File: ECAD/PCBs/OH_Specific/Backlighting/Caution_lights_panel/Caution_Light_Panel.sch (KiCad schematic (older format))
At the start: 30 parts, among them J1 LedCathode, J2 LEDAnnode

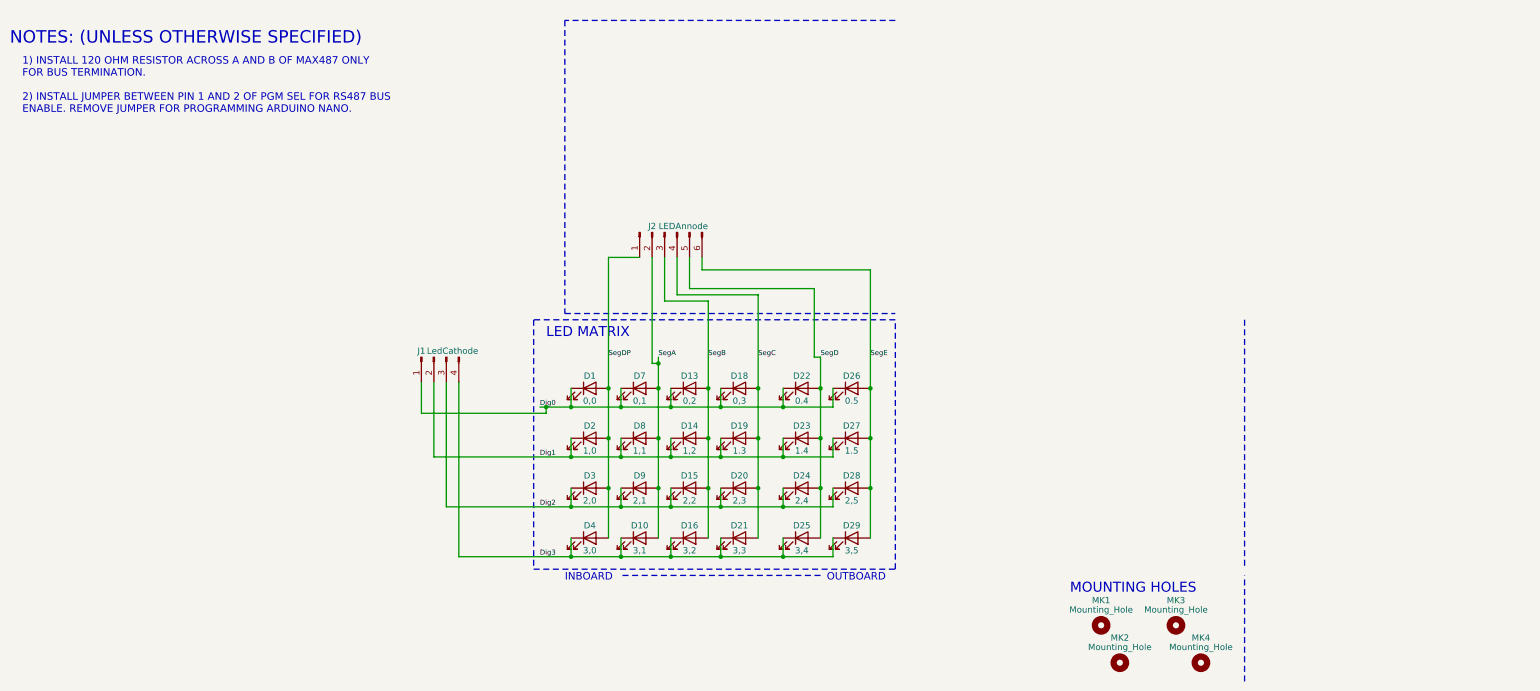
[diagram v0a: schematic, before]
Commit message: Defog Lever Backlighting
Added - Degfog Lever PCB ECAD Files
Added - Defog Lever PCB MCAD Model
Added - Holes in the backplate for the backlighting LEDs
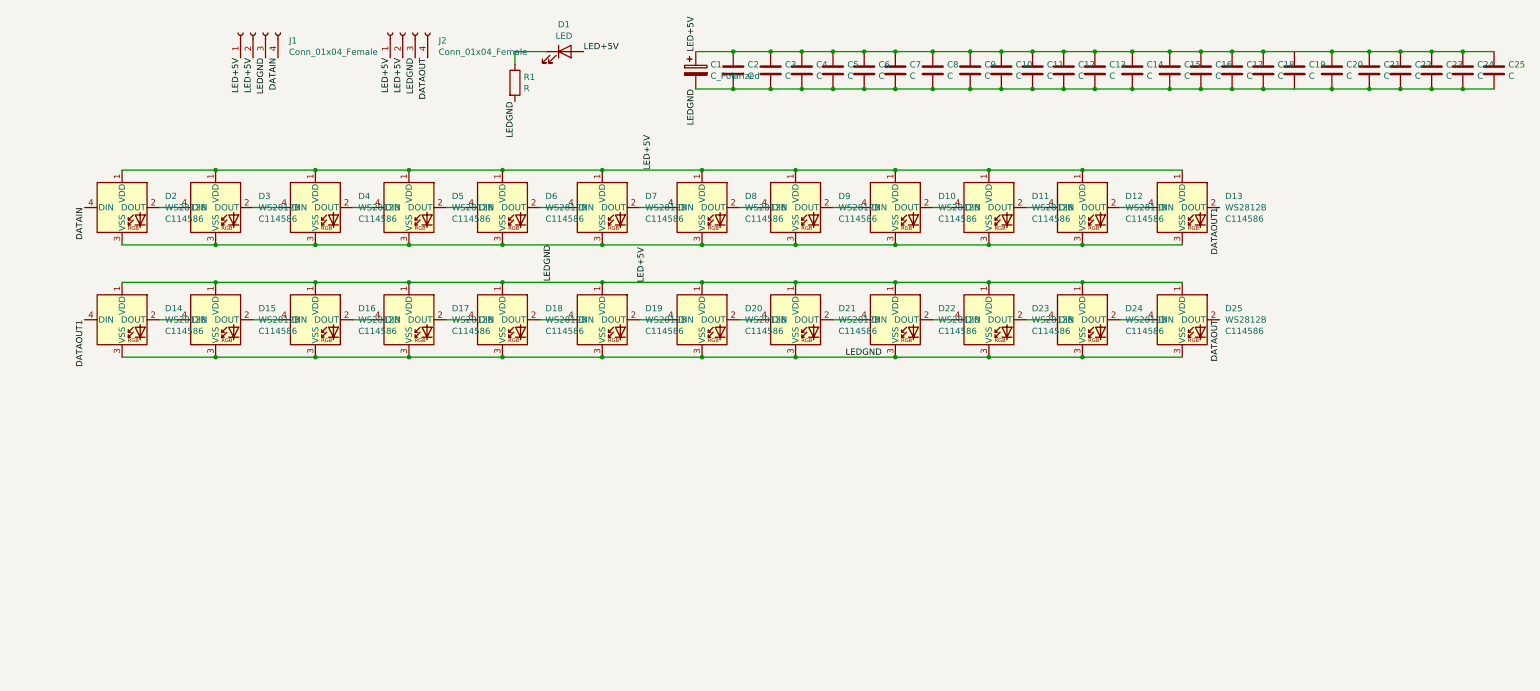
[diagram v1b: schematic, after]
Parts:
- removed D10: 3,1, LED_THT:LED_D3.0mm_FlatTop, symbol Device:LED
- removed D13: 0,2, LED_THT:LED_D3.0mm_FlatTop, symbol Device:LED
- removed D14: 1,2, LED_THT:LED_D3.0mm_FlatTop, symbol Device:LED
- removed D15: 2,2, LED_THT:LED_D3.0mm_FlatTop, symbol Device:LED
- removed D16: 3,2, LED_THT:LED_D3.0mm_FlatTop, symbol Device:LED
- removed D18: 0,3, LED_THT:LED_D3.0mm_FlatTop, symbol Device:LED
- removed D19: 1.3, LED_THT:LED_D3.0mm_FlatTop, symbol Device:LED
- removed D2: 1,0, LED_THT:LED_D3.0mm_FlatTop, symbol Device:LED
- removed D20: 2,3, LED_THT:LED_D3.0mm_FlatTop, symbol Device:LED
- removed D21: 3,3, LED_THT:LED_D3.0mm_FlatTop, symbol Device:LED
- removed D22: 0.4, LED_THT:LED_D3.0mm_FlatTop, symbol Device:LED
- removed D23: 1.4, LED_THT:LED_D3.0mm_FlatTop, symbol Device:LED
- removed D24: 2,4, LED_THT:LED_D3.0mm_FlatTop, symbol Device:LED
- removed D25: 3,4, LED_THT:LED_D3.0mm_FlatTop, symbol Device:LED
- removed D26: 0.5, LED_THT:LED_D3.0mm_FlatTop, symbol Device:LED
- removed D27: 1.5, LED_THT:LED_D3.0mm_FlatTop, symbol Device:LED
- removed D28: 2,5, LED_THT:LED_D3.0mm_FlatTop, symbol Device:LED
- removed D29: 3,5, LED_THT:LED_D3.0mm_FlatTop, symbol Device:LED
- removed D3: 2,0, LED_THT:LED_D3.0mm_FlatTop, symbol Device:LED
- removed D4: 3,0, LED_THT:LED_D3.0mm_FlatTop, symbol Device:LED
- removed D7: 0,1, LED_THT:LED_D3.0mm_FlatTop, symbol Device:LED
- removed D8: 1,1, LED_THT:LED_D3.0mm_FlatTop, symbol Device:LED
- removed D9: 2,1, LED_THT:LED_D3.0mm_FlatTop, symbol Device:LED
- removed J1: LedCathode, PT_Library_v001:Molex_1x04_P2.54mm_Vertical, symbol Connector:Conn_01x04_Male
- removed J2: LEDAnnode, PT_Library_v001:Molex_1x06_P2.54mm_Vertical, symbol Connector:Conn_01x06_Male
- removed MK1, MK2, MK3, MK4: Mounting_Hole, Mounting_Holes:MountingHole_2.5mm, symbol Mechanical:MountingHole
- added C1: C_Polarized, Capacitor_SMD:CP_Elec_8x10, symbol Device:C_Polarized
- added C10, C11, C12, C13, C14, C15, C16, C17, C18, C19, C2, C20, C21, C22, C23, C24, C25, C3, C4, C5, C6, C7, C8, C9: C, Capacitor_SMD:C_0603_1608Metric, symbol Device:C
- added D10, D11, D12, D13, D14, D15, D16, D17, D18, D19, D2, D20, D21, D22, D23, D24, D25, D3, D4, D5, D6, D7, D8, D9: WS2812B, LED_SMD:LED_WS2812B_PLCC4_5.0x5.0mm_P3.2mm, symbol LED:WS2812B
- added J1, J2: Conn_01x04_Female, Connector_Molex:Molex_Mini-Fit_Jr_5566-04A_2x02_P4.20mm_Vertical, symbol Connector:Conn_01x04_Female
- added R1: R, Resistor_SMD:R_0603_1608Metric, symbol Device:R
- D1: value 0,0 -> LED; footprint LED_THT:LED_D3.0mm_FlatTop -> LED_THT:LED_D3.0mm; PN IN-S63AT5UW -> (none)
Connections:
- net Dig0: no longer names the net of D1.1 (K)
- net Dig0: now also R1.1
- net SegDP renamed LED+5V
- net LED+5V: now also C1.1, C10.1, C11.1, C12.1, C13.1, C14.1, C15.1, C16.1, C17.1, C18.1, C19.1, C2.1, C20.1, C21.1, C22.1, C23.1, C24.1, C25.1, C3.1, C4.1, C5.1, C6.1, C7.1, C8.1, C9.1, D10.1 (VDD), D11.1 (VDD), D12.1 (VDD), D13.1 (VDD), D14.1 (VDD), D15.1 (VDD), D16.1 (VDD), D17.1 (VDD), D18.1 (VDD), D19.1 (VDD), D2.1 (VDD), D20.1 (VDD), D21.1 (VDD), D22.1 (VDD), D23.1 (VDD), D24.1 (VDD), D25.1 (VDD), D3.1 (VDD), D4.1 (VDD), D5.1 (VDD), D6.1 (VDD), D7.1 (VDD), D8.1 (VDD), D9.1 (VDD), J1.1 (Pin_1), J1.2 (Pin_2), J2.1 (Pin_1), J2.2 (Pin_2)
- new net: D2.2 (DOUT), D3.4 (DIN)
- new net: D3.2 (DOUT), D4.4 (DIN)
- new net: D4.2 (DOUT), D5.4 (DIN)
- new net: D5.2 (DOUT), D6.4 (DIN)
- new net: D6.2 (DOUT), D7.4 (DIN)
- new net: D7.2 (DOUT), D8.4 (DIN)
- new net: D8.2 (DOUT), D9.4 (DIN)
- new net: D10.4 (DIN), D9.2 (DOUT)
- new net: D10.2 (DOUT), D11.4 (DIN)
- new net: D11.2 (DOUT), D12.4 (DIN)
- new net: D12.2 (DOUT), D13.4 (DIN)
- new net: D14.2 (DOUT), D15.4 (DIN)
- new net: D15.2 (DOUT), D16.4 (DIN)
- new net: D16.2 (DOUT), D17.4 (DIN)
- new net: D17.2 (DOUT), D18.4 (DIN)
- new net: D18.2 (DOUT), D19.4 (DIN)
- new net: D19.2 (DOUT), D20.4 (DIN)
- new net: D20.2 (DOUT), D21.4 (DIN)
- new net: D21.2 (DOUT), D22.4 (DIN)
- new net: D22.2 (DOUT), D23.4 (DIN)
- new net: D23.2 (DOUT), D24.4 (DIN)
- new net: D24.2 (DOUT), D25.4 (DIN)
- new net DATAIN: D2.4 (DIN), J1.4 (Pin_4)
- new net DATAOUT: D25.2 (DOUT), J2.4 (Pin_4)
- new net DATAOUT1: D13.2 (DOUT), D14.4 (DIN)
- new net LEDGND: C1.2, C10.2, C11.2, C12.2, C13.2, C14.2, C15.2, C16.2, C17.2, C18.2, C19.2, C2.2, C20.2, C21.2, C22.2, C23.2, C24.2, C25.2, C3.2, C4.2, C5.2, C6.2, C7.2, C8.2, C9.2, D10.3 (VSS), D11.3 (VSS), D12.3 (VSS), D13.3 (VSS), D14.3 (VSS), D15.3 (VSS), D16.3 (VSS), D17.3 (VSS), D18.3 (VSS), D19.3 (VSS), D2.3 (VSS), D20.3 (VSS), D21.3 (VSS), D22.3 (VSS), D23.3 (VSS), D24.3 (VSS), D25.3 (VSS), D3.3 (VSS), D4.3 (VSS), D5.3 (VSS), D6.3 (VSS), D7.3 (VSS), D8.3 (VSS), D9.3 (VSS), J1.3 (Pin_3), J2.3 (Pin_3), R1.2
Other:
- note removed: "1) INSTALL 120 OHM RESISTOR ACROSS A AND B OF MAX487 ONLY \nFOR BUS TERMINATION.\n\n2) INSTALL JUMPER BETWEEN PIN 1 AND 2 OF PGM SEL FOR RS487 BUS \nENABLE. REMOVE JUMPER FOR PROGRAMMING ARDUINO NANO."
- note removed: "INBOARD"
- note removed: "LED MATRIX"
- note removed: "MOUNTING HOLES"
- note removed: "NOTES: (UNLESS OTHERWISE SPECIFIED)"
- note removed: "OUTBOARD"

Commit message: Latest backlighting changes
Update to multiple PCBs, mainly changing from micro-fit to mini-fit connectors.
Also changing from individual power rails to filled copper planes where possible.
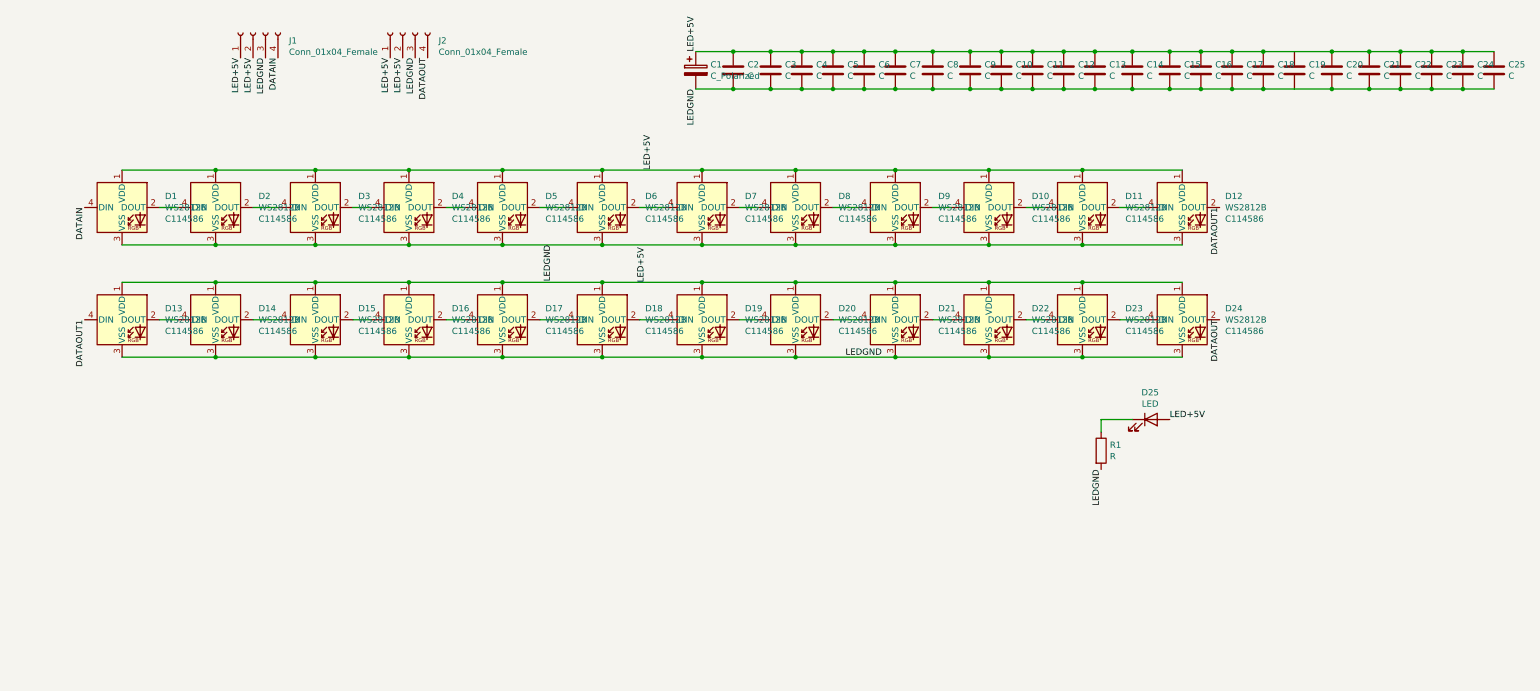
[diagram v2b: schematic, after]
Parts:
- renumbered D2 to D1, D11 to D10, D12 to D11, D13 to D12, D14 to D13, D15 to D14, D16 to D15, D17 to D16, D18 to D17, D19 to D18, D20 to D19, D3 to D2, D21 to D20, D22 to D21, D23 to D22, D24 to D23, D25 to D24, D1 to D25, D4 to D3, D5 to D4, D6 to D5, D7 to D6, D8 to D7, D9 to D8, D10 to D9
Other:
- moved on the sheet: D25, R1
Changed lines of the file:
@@
 L Device:R R1
 U 1 1 5FD9BD6D
-P 4650 1000
-F 0 "R1" H 4720 1046 50  0000 L CNN
-F 1 "R" H 4720 955 50  0000 L CNN
-F 2 "Resistor_SMD:R_0603_1608Metric" V 4580 1000 50  0001 C CNN
-F 3 "~" H 4650 1000 50  0001 C CNN
-	1    4650 1000
-	1    0    0    -1
-$EndComp
-$Comp
-L Device:LED D1
+P 9350 3950
+F 0 "R1" H 9420 3996 50  0000 L CNN
+F 1 "R" H 9420 3905 50  0000 L CNN
+F 2 "Resistor_SMD:R_0603_1608Metric" V 9280 3950 50  0001 C CNN
+F 3 "~" H 9350 3950 50  0001 C CNN
+	1    9350 3950
+	1    0    0    -1
+$EndComp
+$Comp
+L Device:LED D25
 U 1 1 5FD9C14C
-P 5050 750
-F 0 "D1" H 5043 967 50  0000 C CNN
-F 1 "LED" H 5043 876 50  0000 C CNN
-F 2 "LED_THT:LED_D3.0mm" H 5050 750 50  0001 C CNN
-F 3 "~" H 5050 750 50  0001 C CNN
-	1    5050 750
+P 9750 3700
+F 0 "D25" H 9743 3917 50  0000 C CNN
+F 1 "LED" H 9743 3826 50  0000 C CNN
+F 2 "LED_THT:LED_D3.0mm" H 9750 3700 50  0001 C CNN
+F 3 "~" H 9750 3700 50  0001 C CNN
+	1    9750 3700
 	1    0    0    -1
 $EndComp
@@
 DATAOUT
 Wire Wire Line
-	4900 750  4650 750
-Wire Wire Line
-	4650 750  4650 850
-Text Label 5200 750  0    50   ~ 0
+	9600 3700 9350 3700
+Wire Wire Line
+	9350 3700 9350 3800
+Text Label 9900 3700 0    50   ~ 0
 LED+5V
-Text Label 4650 1150 3    50   ~ 0
+Text Label 9350 4100 3    50   ~ 0
 LEDGND
 Text Label 6100 1050 3    50   ~ 0
@@
 LED+5V
 $Comp
-L LED:WS2812B D8
+L LED:WS2812B D7
 U 1 1 5FDA82D3
 P 6150 2000
-F 0 "D8" H 6494 2091 50  0000 L CNN
+F 0 "D7" H 6494 2091 50  0000 L CNN
 F 1 "WS2812B" H 6494 2000 50  0000 L CNN
 F 2 "LED_SMD:LED_WS2812B_PLCC4_5.0x5.0mm_P3.2mm" H 6200 1700 50  0001 L TNN
@@
 $EndComp
 $Comp
-L LED:WS2812B D9
+L LED:WS2812B D8
 U 1 1 5FDA82DA
 P 6900 2000
-F 0 "D9" H 7244 2091 50  0000 L CNN
+F 0 "D8" H 7244 2091 50  0000 L CNN
 F 1 "WS2812B" H 7244 2000 50  0000 L CNN
 F 2 "LED_SMD:LED_WS2812B_PLCC4_5.0x5.0mm_P3.2mm" H 6950 1700 50  0001 L TNN
@@
 $EndComp
 $Comp
-L LED:WS2812B D10
+L LED:WS2812B D9
 U 1 1 5FDA82E1
 P 7700 2000
-F 0 "D10" H 8044 2091 50  0000 L CNN
+F 0 "D9" H 8044 2091 50  0000 L CNN
 F 1 "WS2812B" H 8044 2000 50  0000 L CNN
 F 2 "LED_SMD:LED_WS2812B_PLCC4_5.0x5.0mm_P3.2mm" H 7750 1700 50  0001 L TNN
@@
 $EndComp
 $Comp
-L LED:WS2812B D11
+L LED:WS2812B D10
 U 1 1 5FDA82E8
 P 8450 2000
-F 0 "D11" H 8794 2091 50  0000 L CNN
+F 0 "D10" H 8794 2091 50  0000 L CNN
 F 1 "WS2812B" H 8794 2000 50  0000 L CNN
 F 2 "LED_SMD:LED_WS2812B_PLCC4_5.0x5.0mm_P3.2mm" H 8500 1700 50  0001 L TNN
@@
 $EndComp
 $Comp
-L LED:WS2812B D12
+L LED:WS2812B D11
 U 1 1 5FDA82EF
 P 9200 2000
-F 0 "D12" H 9544 2091 50  0000 L CNN
+F 0 "D11" H 9544 2091 50  0000 L CNN
 F 1 "WS2812B" H 9544 2000 50  0000 L CNN
 F 2 "LED_SMD:LED_WS2812B_PLCC4_5.0x5.0mm_P3.2mm" H 9250 1700 50  0001 L TNN
@@
 $EndComp
 $Comp
-L LED:WS2812B D13
+L LED:WS2812B D12
 U 1 1 5FDA82F6
 P 10000 2000
-F 0 "D13" H 10344 2091 50  0000 L CNN
+F 0 "D12" H 10344 2091 50  0000 L CNN
 F 1 "WS2812B" H 10344 2000 50  0000 L CNN
 F 2 "LED_SMD:LED_WS2812B_PLCC4_5.0x5.0mm_P3.2mm" H 10050 1700 50  0001 L TNN
@@
 $EndComp
 $Comp
-L LED:WS2812B D14
+L LED:WS2812B D13
 U 1 1 5FDB44DF
 P 1500 2900
-F 0 "D14" H 1844 2991 50  0000 L CNN
+F 0 "D13" H 1844 2991 50  0000 L CNN
 F 1 "WS2812B" H 1844 2900 50  0000 L CNN
 F 2 "LED_SMD:LED_WS2812B_PLCC4_5.0x5.0mm_P3.2mm" H 1550 2600 50  0001 L TNN
@@
 $EndComp
 $Comp
-L LED:WS2812B D15
+L LED:WS2812B D14
 U 1 1 5FDB44E6
 P 2250 2900
-F 0 "D15" H 2594 2991 50  0000 L CNN
+F 0 "D14" H 2594 2991 50  0000 L CNN
 F 1 "WS2812B" H 2594 2900 50  0000 L CNN
 F 2 "LED_SMD:LED_WS2812B_PLCC4_5.0x5.0mm_P3.2mm" H 2300 2600 50  0001 L TNN
@@
 $EndComp
 $Comp
-L LED:WS2812B D24
+L LED:WS2812B D23
 U 1 1 5FDB4525
 P 9200 2900
-F 0 "D24" H 9544 2991 50  0000 L CNN
+F 0 "D23" H 9544 2991 50  0000 L CNN
 F 1 "WS2812B" H 9544 2900 50  0000 L CNN
 F 2 "LED_SMD:LED_WS2812B_PLCC4_5.0x5.0mm_P3.2mm" H 9250 2600 50  0001 L TNN
@@
 $EndComp
 $Comp
-L LED:WS2812B D25
+L LED:WS2812B D24
 U 1 1 5FDB452C
 P 10000 2900
-F 0 "D25" H 10344 2991 50  0000 L CNN
+F 0 "D24" H 10344 2991 50  0000 L CNN
 F 1 "WS2812B" H 10344 2900 50  0000 L CNN
 F 2 "LED_SMD:LED_WS2812B_PLCC4_5.0x5.0mm_P3.2mm" H 10050 2600 50  0001 L TNN
@@
 	6150 3200 6900 3200
 $Comp
-L LED:WS2812B D23
+L LED:WS2812B D22
 U 1 1 5FDB451E
 P 8450 2900
-F 0 "D23" H 8794 2991 50  0000 L CNN
+F 0 "D22" H 8794 2991 50  0000 L CNN
 F 1 "WS2812B" H 8794 2900 50  0000 L CNN
 F 2 "LED_SMD:LED_WS2812B_PLCC4_5.0x5.0mm_P3.2mm" H 8500 2600 50  0001 L TNN
@@
 $EndComp
 $Comp
-L LED:WS2812B D22
+L LED:WS2812B D21
 U 1 1 5FDB4517
 P 7700 2900
-F 0 "D22" H 8044 2991 50  0000 L CNN
+F 0 "D21" H 8044 2991 50  0000 L CNN
 F 1 "WS2812B" H 8044 2900 50  0000 L CNN
 F 2 "LED_SMD:LED_WS2812B_PLCC4_5.0x5.0mm_P3.2mm" H 7750 2600 50  0001 L TNN
@@
 $EndComp
 $Comp
-L LED:WS2812B D21
+L LED:WS2812B D20
 U 1 1 5FDB4510
 P 6900 2900
-F 0 "D21" H 7244 2991 50  0000 L CNN
+F 0 "D20" H 7244 2991 50  0000 L CNN
 F 1 "WS2812B" H 7244 2900 50  0000 L CNN
 F 2 "LED_SMD:LED_WS2812B_PLCC4_5.0x5.0mm_P3.2mm" H 6950 2600 50  0001 L TNN
@@
 $EndComp
 $Comp
-L LED:WS2812B D20
+L LED:WS2812B D19
 U 1 1 5FDB4509
 P 6150 2900
-F 0 "D20" H 6494 2991 50  0000 L CNN
+F 0 "D19" H 6494 2991 50  0000 L CNN
 F 1 "WS2812B" H 6494 2900 50  0000 L CNN
 F 2 "LED_SMD:LED_WS2812B_PLCC4_5.0x5.0mm_P3.2mm" H 6200 2600 50  0001 L TNN
@@
 	2250 2300 3050 2300
 $Comp
-L LED:WS2812B D2
+L LED:WS2812B D1
 U 1 1 5FD9AE44
 P 1500 2000
-F 0 "D2" H 1844 2091 50  0000 L CNN
+F 0 "D1" H 1844 2091 50  0000 L CNN
 F 1 "WS2812B" H 1844 2000 50  0000 L CNN
 F 2 "LED_SMD:LED_WS2812B_PLCC4_5.0x5.0mm_P3.2mm" H 1550 1700 50  0001 L TNN
@@
 DATAIN
 $Comp
-L LED:WS2812B D3
+L LED:WS2812B D2
 U 1 1 5FDA3196
 P 2250 2000
-F 0 "D3" H 2594 2091 50  0000 L CNN
+F 0 "D2" H 2594 2091 50  0000 L CNN
 F 1 "WS2812B" H 2594 2000 50  0000 L CNN
 F 2 "LED_SMD:LED_WS2812B_PLCC4_5.0x5.0mm_P3.2mm" H 2300 1700 50  0001 L TNN
@@
 Connection ~ 5350 1700
 $Comp
-L LED:WS2812B D4
+L LED:WS2812B D3
 U 1 1 5FDA3664
 P 3050 2000
-F 0 "D4" H 3394 2091 50  0000 L CNN
+F 0 "D3" H 3394 2091 50  0000 L CNN
 F 1 "WS2812B" H 3394 2000 50  0000 L CNN
 F 2 "LED_SMD:LED_WS2812B_PLCC4_5.0x5.0mm_P3.2mm" H 3100 1700 50  0001 L TNN
@@
 	3050 2300 3800 2300
 $Comp
-L LED:WS2812B D5
+L LED:WS2812B D4
 U 1 1 5FDA3A08
 P 3800 2000
-F 0 "D5" H 4144 2091 50  0000 L CNN
+F 0 "D4" H 4144 2091 50  0000 L CNN
 F 1 "WS2812B" H 4144 2000 50  0000 L CNN
 F 2 "LED_SMD:LED_WS2812B_PLCC4_5.0x5.0mm_P3.2mm" H 3850 1700 50  0001 L TNN
@@
 $EndComp
 $Comp
-L LED:WS2812B D6
+L LED:WS2812B D5
 U 1 1 5FDA3E90
 P 4550 2000
-F 0 "D6" H 4894 2091 50  0000 L CNN
+F 0 "D5" H 4894 2091 50  0000 L CNN
 F 1 "WS2812B" H 4894 2000 50  0000 L CNN
 F 2 "LED_SMD:LED_WS2812B_PLCC4_5.0x5.0mm_P3.2mm" H 4600 1700 50  0001 L TNN
@@
 $EndComp
 $Comp
-L LED:WS2812B D16
+L LED:WS2812B D15
 U 1 1 5FDB44ED
 P 3050 2900
-F 0 "D16" H 3394 2991 50  0000 L CNN
+F 0 "D15" H 3394 2991 50  0000 L CNN
 F 1 "WS2812B" H 3394 2900 50  0000 L CNN
 F 2 "LED_SMD:LED_WS2812B_PLCC4_5.0x5.0mm_P3.2mm" H 3100 2600 50  0001 L TNN
@@
 $EndComp
 $Comp
-L LED:WS2812B D17
+L LED:WS2812B D16
 U 1 1 5FDB44F4
 P 3800 2900
-F 0 "D17" H 4144 2991 50  0000 L CNN
+F 0 "D16" H 4144 2991 50  0000 L CNN
 F 1 "WS2812B" H 4144 2900 50  0000 L CNN
 F 2 "LED_SMD:LED_WS2812B_PLCC4_5.0x5.0mm_P3.2mm" H 3850 2600 50  0001 L TNN
@@
 $EndComp
 $Comp
-L LED:WS2812B D18
+L LED:WS2812B D17
 U 1 1 5FDB44FB
 P 4550 2900
-F 0 "D18" H 4894 2991 50  0000 L CNN
+F 0 "D17" H 4894 2991 50  0000 L CNN
 F 1 "WS2812B" H 4894 2900 50  0000 L CNN
 F 2 "LED_SMD:LED_WS2812B_PLCC4_5.0x5.0mm_P3.2mm" H 4600 2600 50  0001 L TNN
@@
 Connection ~ 4550 3200
 $Comp
-L LED:WS2812B D19
+L LED:WS2812B D18
 U 1 1 5FDB4502
 P 5350 2900
-F 0 "D19" H 5694 2991 50  0000 L CNN
+F 0 "D18" H 5694 2991 50  0000 L CNN
 F 1 "WS2812B" H 5694 2900 50  0000 L CNN
 F 2 "LED_SMD:LED_WS2812B_PLCC4_5.0x5.0mm_P3.2mm" H 5400 2600 50  0001 L TNN
@@
 	3500 2900 3350 2900
 $Comp
-L LED:WS2812B D7
+L LED:WS2812B D6
 U 1 1 5FDA41A2
 P 5350 2000
-F 0 "D7" H 5694 2091 50  0000 L CNN
+F 0 "D6" H 5694 2091 50  0000 L CNN
 F 1 "WS2812B" H 5694 2000 50  0000 L CNN
 F 2 "LED_SMD:LED_WS2812B_PLCC4_5.0x5.0mm_P3.2mm" H 5400 1700 50  0001 L TNN
